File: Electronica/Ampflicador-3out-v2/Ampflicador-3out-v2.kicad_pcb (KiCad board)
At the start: 2 copper layers, 32 parts, among them Q1 MPF102, U1 LM386

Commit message: Amp v2
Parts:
- R1, R2, R3, R4, R5, R6: footprint Resistor_THT:R_Axial_DIN0204_L3.6mm_D1.6mm_P5.08mm_Horizontal -> Resistor_THT:R_Axial_DIN0204_L3.6mm_D1.6mm_P7.62mm_Horizontal
- moved ? 82.5 mm to (23.0, 14.5)
- moved ? 82.5 mm to (23.1, 45.6)
- moved Power-Input1 18.4 mm to (42.6, 17.5), turned to 180 degrees
- moved R5 14.2 mm to (35.4, 28.0), turned to 0 degrees
- moved C12 12.9 mm to (52.0, 27.5), turned to 0 degrees
- moved R6 12.3 mm to (35.4, 25.5), turned to 0 degrees
- moved C10 9.59 mm to (51.6, 40.2), turned to 0 degrees
- moved Piezo-Input1 8.54 mm to (39.7, 39.5), turned to -90 degrees
- moved C11 7.20 mm to (51.6, 33.3), turned to 0 degrees
- moved R4 6.97 mm to (43.0, 30.5), turned to 180 degrees
- moved Q1 4.34 mm to (49.0, 27.6), turned to 180 degrees
- moved R3 3.18 mm to (43.0, 33.0), turned to 180 degrees
- moved R2 2.48 mm to (71.0, 38.0)
- moved C5 2.00 mm to (73.5, 41.5)
- moved C2 1.57 mm to (82.2, 39.5), turned to 180 degrees
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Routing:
- net Net-(Power-Input1-Pin_2): track 47.6 -> 111.5 mm
- net Net-(Q1-G): track 0.00 -> 63.1 mm
- net Net-(Vol1-Pin_1): track 32.4 -> 13.9 mm
- net Net-(C11-Pad1): track 11.3 -> 27.4 mm
- net Net-(Q1-D): track 22.8 -> 14.2 mm
- net Net-(Piezo-Input1-Pin_2): track 9.34 -> 16.2 mm
- net Net-(C7-Pad2): track 6.18 -> 4.01 mm

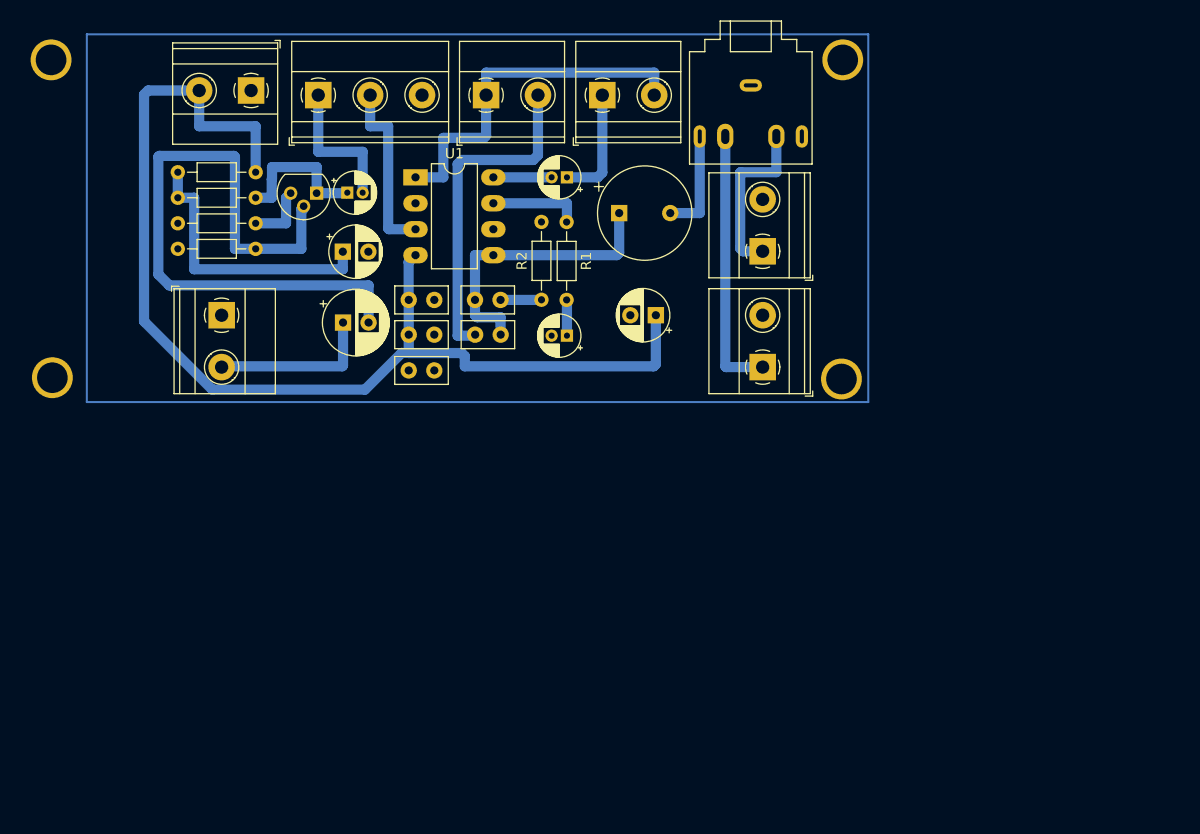
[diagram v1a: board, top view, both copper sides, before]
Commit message: Amp v2 terminada - sin molex
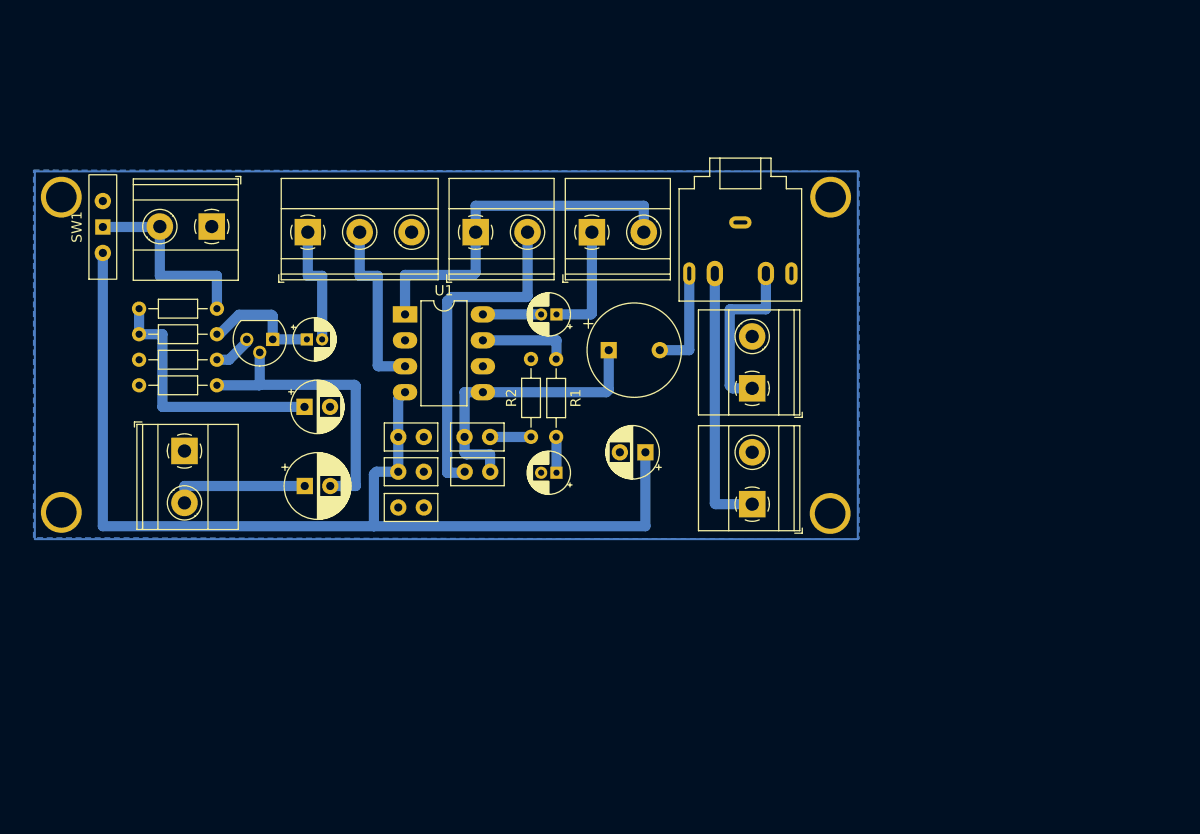
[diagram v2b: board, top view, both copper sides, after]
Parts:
- added SW1: SW_DPST_x2, Button_Switch_THT:SW_Slide-03_Wuerth-WS-SLTV_10x2.5x6.4_P2.54mm, F.Cu at (28.1, 30.9)
- moved C10 16.4 mm to (47.8, 56.2)
- moved C11 15.6 mm to (47.8, 48.5)
- moved Q1 14.9 mm to (44.7, 41.9)
- moved C12 14.9 mm to (48.0, 41.9)
- moved R5 13.9 mm to (31.6, 41.4)
- moved R6 13.9 mm to (31.6, 38.9)
- moved R4 13.9 mm to (39.2, 43.9)
- moved R3 13.9 mm to (39.2, 46.4)
- moved Power-Input1 13.9 mm to (38.7, 30.8)
- moved Piezo-Input1 13.8 mm to (36.1, 52.8)
- moved ? 13.5 mm to (99.3, 27.9)
- moved ? 13.5 mm to (24.0, 27.9)
- moved Output-Jack-6.1 13.5 mm to (91.6, 46.7)
- moved R2 13.5 mm to (70.0, 51.4)
- moved Bass1 13.5 mm to (64.6, 31.4)
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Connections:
- C1 pad 1: Net-(Power-Input1-Pin_2) -> Net-(SW1A-B)
- C2 pad 1: Net-(Power-Input1-Pin_2) -> Net-(SW1A-B)
- C3 pad 2: Net-(Power-Input1-Pin_2) -> Net-(SW1A-B)
- Output-Jack-3.1 pad RN: Net-(Output-Jack-6.1-Pin_1) -> (no net)
- Output-Jack-3.1 pad S: GND -> unconnected-(Output-Jack-3.1-PadS)
- R6 pad 2: Net-(Power-Input1-Pin_2) -> Net-(SW1A-B)
- U1 pad 4: Net-(Power-Input1-Pin_2) -> Net-(SW1A-B)
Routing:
- net Net-(SW1A-B): track 0.00 -> 103.1 mm
- net Net-(Power-Input1-Pin_2): track 111.5 -> 19.2 mm
- net Net-(Q1-G): track 63.1 -> 28.8 mm
- net Net-(Piezo-Input1-Pin_2): track 16.2 -> 13.4 mm
- net Net-(Q1-D): track 14.2 -> 11.9 mm
- net Net-(Q1-S): track 6.11 -> 3.89 mm
- net Net-(Vol1-Pin_1): track 13.9 -> 11.9 mm
- net Net-(C11-Pad1): track 27.4 -> 25.8 mm
- net Net-(Bass1-Pin_1): track 35.7 -> 36.5 mm
- added copper zone on B.Cu, net GND

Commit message: Amp v2 sin terminar - con molex
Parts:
- Bass1, Gain1, Output-Jack-6.1, Output-Speaker1, Piezo-Input1, Power-Input1: footprint TerminalBlock_Phoenix:TerminalBlock_Phoenix_MKDS-1,5-2-5.08_1x02_P5.08mm_Horizontal -> Connector_Molex:Molex_KK-254_AE-6410-02A_1x02_P2.54mm_Vertical
- Output-Jack-3.1: footprint Connector_Audio:Jack_3.5mm_CUI_SJ1-3525N_Horizontal -> Connector_Molex:Molex_KK-254_AE-6410-05A_1x05_P2.54mm_Vertical
- SW1: footprint Button_Switch_THT:SW_Slide-03_Wuerth-WS-SLTV_10x2.5x6.4_P2.54mm -> Connector_Molex:Molex_KK-254_AE-6410-02A_1x02_P2.54mm_Vertical
- Vol1: footprint TerminalBlock_Phoenix:TerminalBlock_Phoenix_MKDS-1,5-3-5.08_1x03_P5.08mm_Horizontal -> Connector_Molex:Molex_KK-254_AE-6410-03A_1x03_P2.54mm_Vertical
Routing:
- removed copper zone on B.Cu, net GND

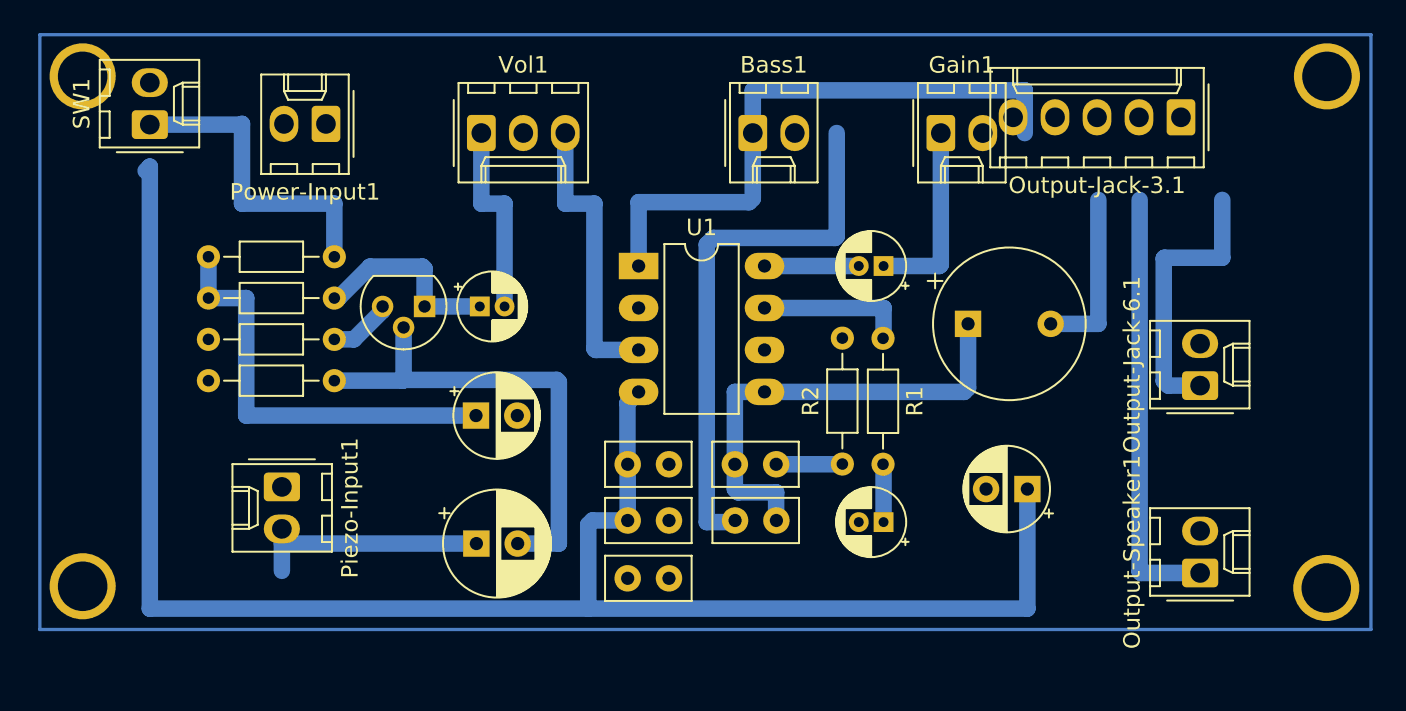
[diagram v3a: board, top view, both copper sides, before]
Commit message: PCB Amp v2 terminada - Molex
Plano de masa
Conectores Molex
3 piezos
Suma de señales de entrada
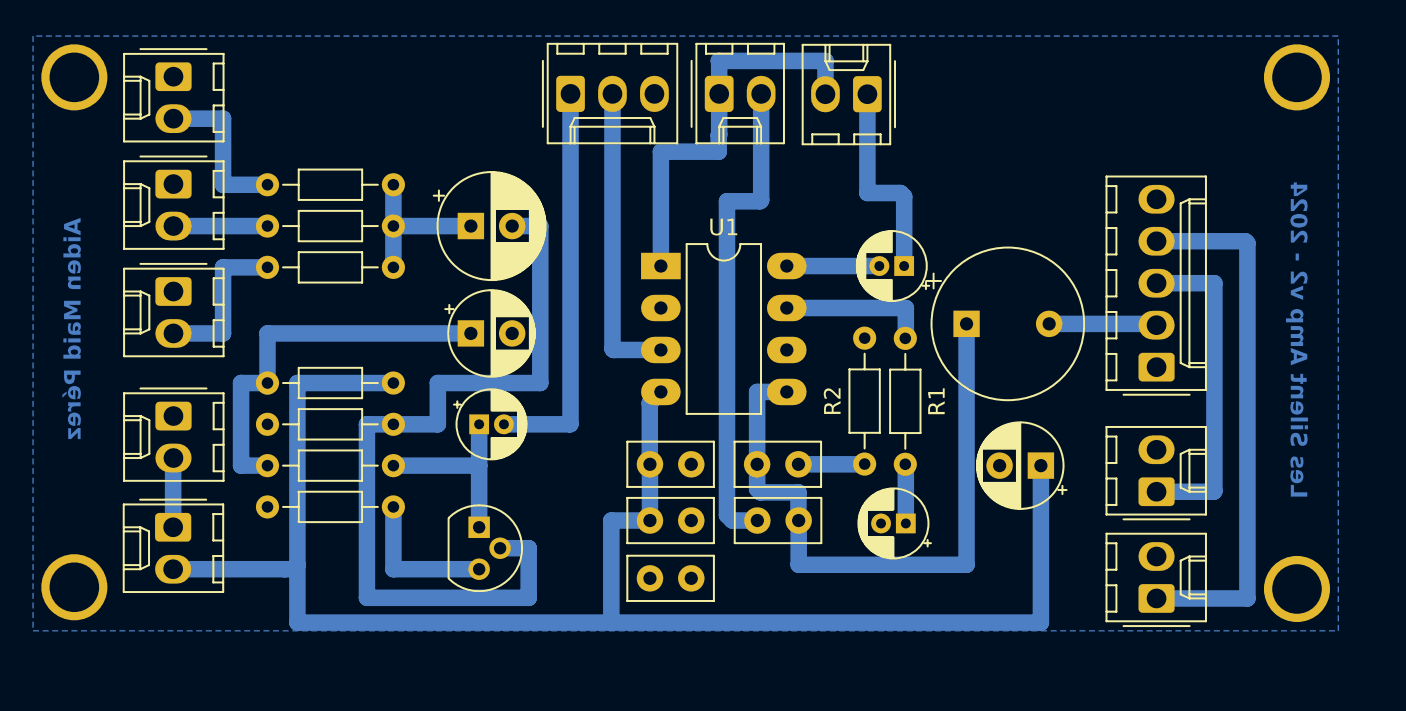
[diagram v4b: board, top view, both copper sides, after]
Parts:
- added Input2: Screw_Terminal_01x02, Connector_Molex:Molex_KK-254_AE-6410-02A_1x02_P2.54mm_Vertical, F.Cu at (29.5, 28.0)
- added Input3: Screw_Terminal_01x02, Connector_Molex:Molex_KK-254_AE-6410-02A_1x02_P2.54mm_Vertical, F.Cu at (29.5, 41.0)
- added R7: 100Ω, Resistor_THT:R_Axial_DIN0204_L3.6mm_D1.6mm_P7.62mm_Horizontal, F.Cu at (35.2, 34.5)
- added R8: 100Ω, Resistor_THT:R_Axial_DIN0204_L3.6mm_D1.6mm_P7.62mm_Horizontal, F.Cu at (35.2, 37.0)
- added R9: 100Ω, Resistor_THT:R_Axial_DIN0204_L3.6mm_D1.6mm_P7.62mm_Horizontal, F.Cu at (35.2, 39.5)
- moved SW1 24.4 mm to (29.5, 55.2), turned to -90 degrees
- moved Power-Input1 19.9 mm to (29.5, 48.5), turned to -90 degrees
- moved Input1 19.5 mm to (29.5, 34.5)
- moved C10 19.2 mm to (47.5, 37.0)
- moved Output-Jack-3.1 15.2 mm to (89.0, 45.5), turned to 90 degrees
- moved Q1 13.8 mm to (48.0, 55.2), turned to -90 degrees
- moved Output-Jack-6.1 13.1 mm to (89.0, 59.5)
- moved R4 10.8 mm to (42.8, 54.0)
- moved R5 10.8 mm to (35.2, 51.5)
- moved R6 8.44 mm to (35.2, 46.5)
- moved C12 7.13 mm to (48.0, 49.0)
- moved Vol1 5.89 mm to (53.5, 29.0)
- moved Output-Speaker1 5.58 mm to (89.0, 53.1)
- moved Gain1 5.03 mm to (71.5, 29.0), turned to 180 degrees
- moved C11 4.98 mm to (47.5, 43.5)
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- renumbered Piezo-Input1 to Input1
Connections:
- ? pad : (no net) -> GND (x4)
- C10 pad 1: Net-(Piezo-Input1-Pin_2) -> Net-(C10-Pad1)
- Input1 pad 2: Net-(Piezo-Input1-Pin_2) -> Net-(Input1-Pin_2)
- Output-Jack-3.1 pad 1: (no net) -> GND
- Output-Jack-3.1 pad 2: (no net) -> Net-(C9-Pad2)
- Output-Jack-3.1 pad 3: (no net) -> Net-(Output-Speaker1-Pin_1)
- Output-Jack-3.1 pad 4: (no net) -> Net-(Output-Jack-6.1-Pin_1)
- Output-Jack-3.1 pad 5: (no net) -> GND
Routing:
- net Net-(Q1-G): track 28.8 -> 48.9 mm
- net Net-(Output-Jack-6.1-Pin_1): track 16.8 -> 32.5 mm
- net Net-(Power-Input1-Pin_2): track 19.2 -> 4.20 mm
- net Net-(Piezo-Input1-Pin_2): track 13.4 -> 0.00 mm
- net Net-(Vol1-Pin_1): track 11.9 -> 24.0 mm
- net Net-(Bass1-Pin_1): track 36.5 -> 24.5 mm
- net Net-(C7-Pad1): track 28.3 -> 39.4 mm
- net Net-(Input2-Pin_2): track 0.00 -> 9.79 mm
- net Net-(Input3-Pin_2): track 0.00 -> 9.69 mm
- net Net-(C10-Pad1): track 0.00 -> 9.69 mm
- net Net-(Output-Speaker1-Pin_1): track 26.2 -> 19.6 mm
- net Net-(Input1-Pin_2): track 0.00 -> 5.69 mm
- net Net-(Q1-S): track 3.89 -> 8.96 mm
- net Net-(SW1A-B): track 103.1 -> 99.0 mm
- net Net-(C9-Pad2): track 10.4 -> 6.65 mm
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- added copper zone on B.Cu, net GND
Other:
- board text added: "Aiden Maid Pérez"
- board text added: "Les Silent Amp v2 - 2024"

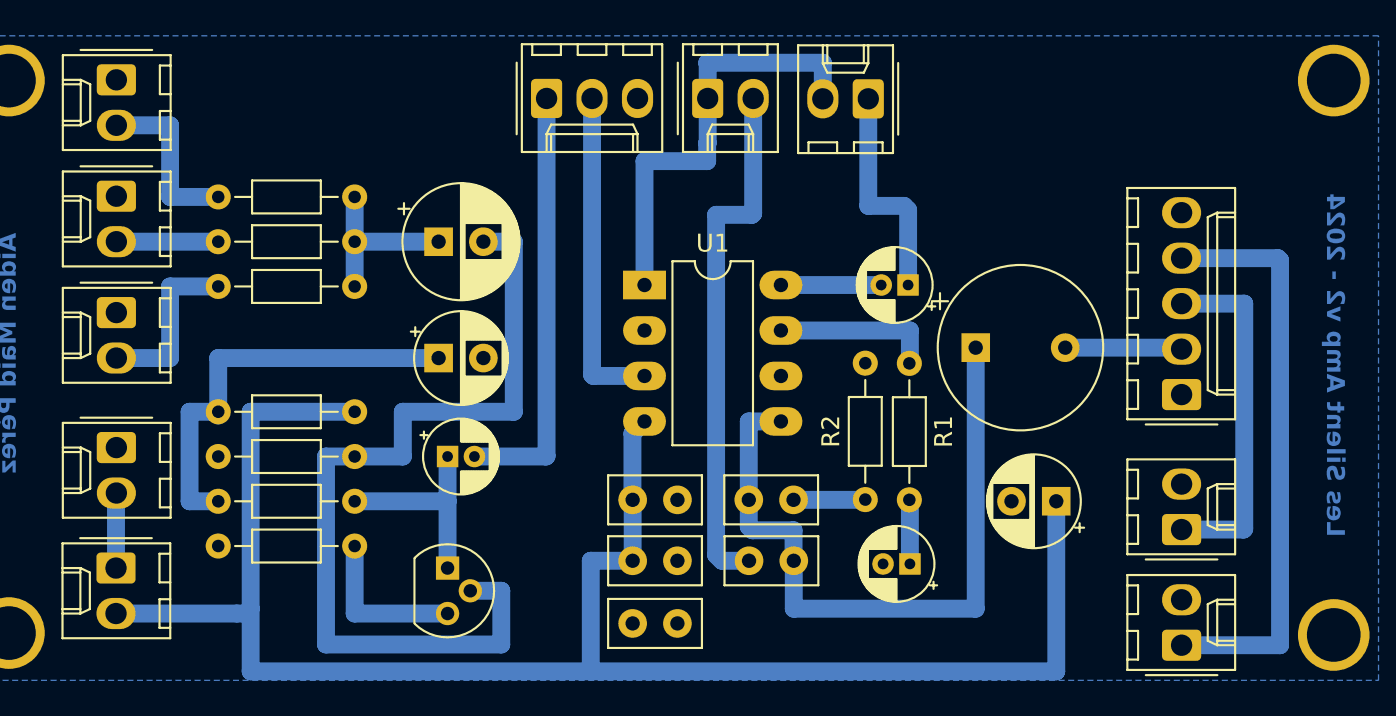
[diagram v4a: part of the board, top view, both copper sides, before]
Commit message: Amp v2 - Molex y pistas 45°
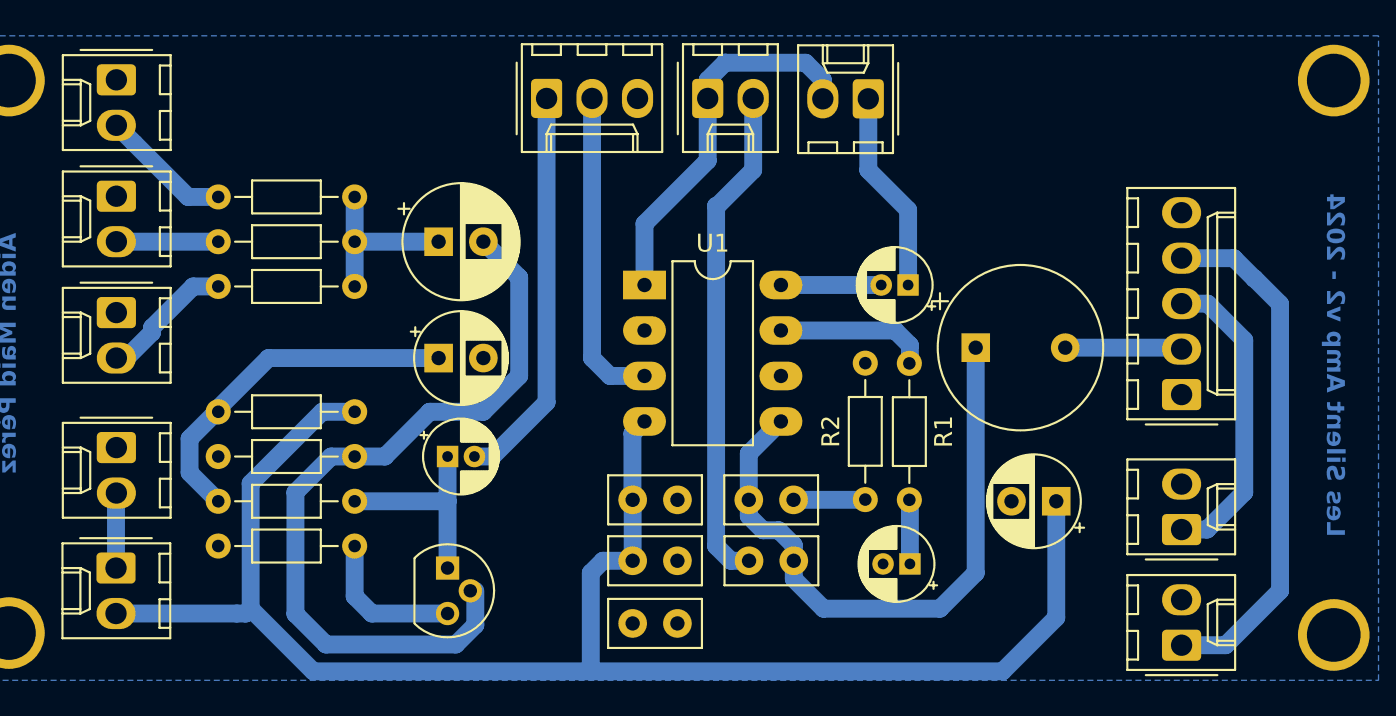
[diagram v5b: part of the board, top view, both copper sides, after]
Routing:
- net Net-(SW1A-B): track 99.0 -> 92.5 mm
- net Net-(Q1-G): track 48.9 -> 43.4 mm
- net Net-(C7-Pad1): track 39.4 -> 35.4 mm
- net Net-(C11-Pad1): track 23.5 -> 20.1 mm
- net Net-(Output-Jack-6.1-Pin_1): track 32.5 -> 29.3 mm
- net Net-(Bass1-Pin_1): track 24.5 -> 21.3 mm
- net Net-(Output-Speaker1-Pin_1): track 19.6 -> 17.2 mm
- net Net-(Input2-Pin_2): track 9.79 -> 7.45 mm
- net Net-(Input3-Pin_2): track 9.69 -> 7.50 mm
- net Net-(Vol1-Pin_1): track 24.0 -> 22.3 mm
- net Net-(Bass1-Pin_2): track 29.5 -> 28.1 mm
- net Net-(Gain1-Pin_1): track 12.5 -> 11.3 mm
- net Net-(Q1-S): track 8.96 -> 8.40 mm
- net Net-(U1-+): track 18.4 -> 17.8 mm
